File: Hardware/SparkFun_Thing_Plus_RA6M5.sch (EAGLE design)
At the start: 109 parts, among them J1 USB Female Type C Connector, J2 THING_PLUS_LOGICAL, J3 QWIIC_RA, J4 CONN_03X2, J7 MICRO-SDFRICTION, Q1 20V/4.2A/52mΩ/1.4W, Q2 20V/4.2A/52mΩ/1.4W, U1 R7FA6M5, U2 DA14531MOD, U3 MCP73831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

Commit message: Update for Reds.
Change QSPI flash chip to same one as Portenta C33
Remove boot button
Move reset button to space it out
Add boot test point
Recenter programming header silk
Update GPIO silk
Rename nets in schematic
Remove BLE Reset jumper
Remove DNP caps from 24MHz xtal
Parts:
- removed C7, C8: DNP, SparkFun-Capacitors:DNP-0402-TIGHT_NO_CREAM
- removed RST: JUMPER-SMT_2_NC_TRACE_SILK, SparkFun-Jumpers:JUMPER-SMT_2_NC_TRACE_SILK
- removed S1: BOOT, SparkFun-Switches:MOMENTARY-SWITCH-SPST-SMD-4.6X2.8MM
- added TP10: TEST-POINT3X5, SparkFun-Connectors:TEST-POINT3X5
- FRAME1, FRAME2: REV v01 -> v10
- U5: value W25QXX128MBIT-6X5 -> MX25L12833F 128Mb; device SparkFun-IC-Memory:W25QXX128MBIT-6X5 -> SparkFun-IC-Memory:MX25L12833F_128MBIT_QSPI
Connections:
- net A0 renamed A0/DAC0/D7
- net A1 renamed A1/DAC1/D8
- net A2 renamed A2/D9
- net A3 renamed A3/D10
- net A4 renamed A4/D11
- net A5 renamed A5/D12
- net DA14531_RST renamed BLE_RST
- net FREE renamed FREE/D30
- net GPIO0/!CS! renamed GPIO0/!CS!/D0
- net GPIO1 renamed GPIO1/D1
- net GPIO2 renamed GPIO2/D2
- net GPIO3 renamed GPIO3/D3
- net GPIO4 renamed GPIO4/D4
- net GPIO5 renamed GPIO5/D5
- net GPIO6 renamed GPIO6/D6
- net RA6_SWO/TDO/PICO renamed RA6_SWO/TDO/PICO/D18
- net RA6_TDI/POCI renamed RA6_TDI/POCI/D17
- net SCK renamed SCK/D19
- net SCL renamed SCL/D16
- net SDA renamed SDA/D15
- net UART_RX renamed UART_RX/D21
- net UART_TX renamed UART_TX/D20
- removed net N$25: RST.2, U1G1.P115/SSITXD0_B/GTIOC4A
- net !DA14531_RST!: now also U1G1.P115/SSITXD0_B/GTIOC4A; no longer RST.1
- net BOOT/MD: now also TP10.1; no longer S1.2
- net EXTAL: no longer C7.2
- net GND: no longer S1.1
- net GND_24: no longer C7.1, C8.1
- net QIO3: now also U5.D3/!RESET!; no longer U5.D3/!HOLD!
- net XTAL: no longer C8.2
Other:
- note added: "To load a new bootloader, pull BOOT/MD low. To load new Arduino code, double tap reset button."
- note removed: "Cut RST trace to remove BLE module reset capability. In case doing this causes a boot loop. To be removed or disabled in reds."
- moved on the sheet: R14, R8, S2

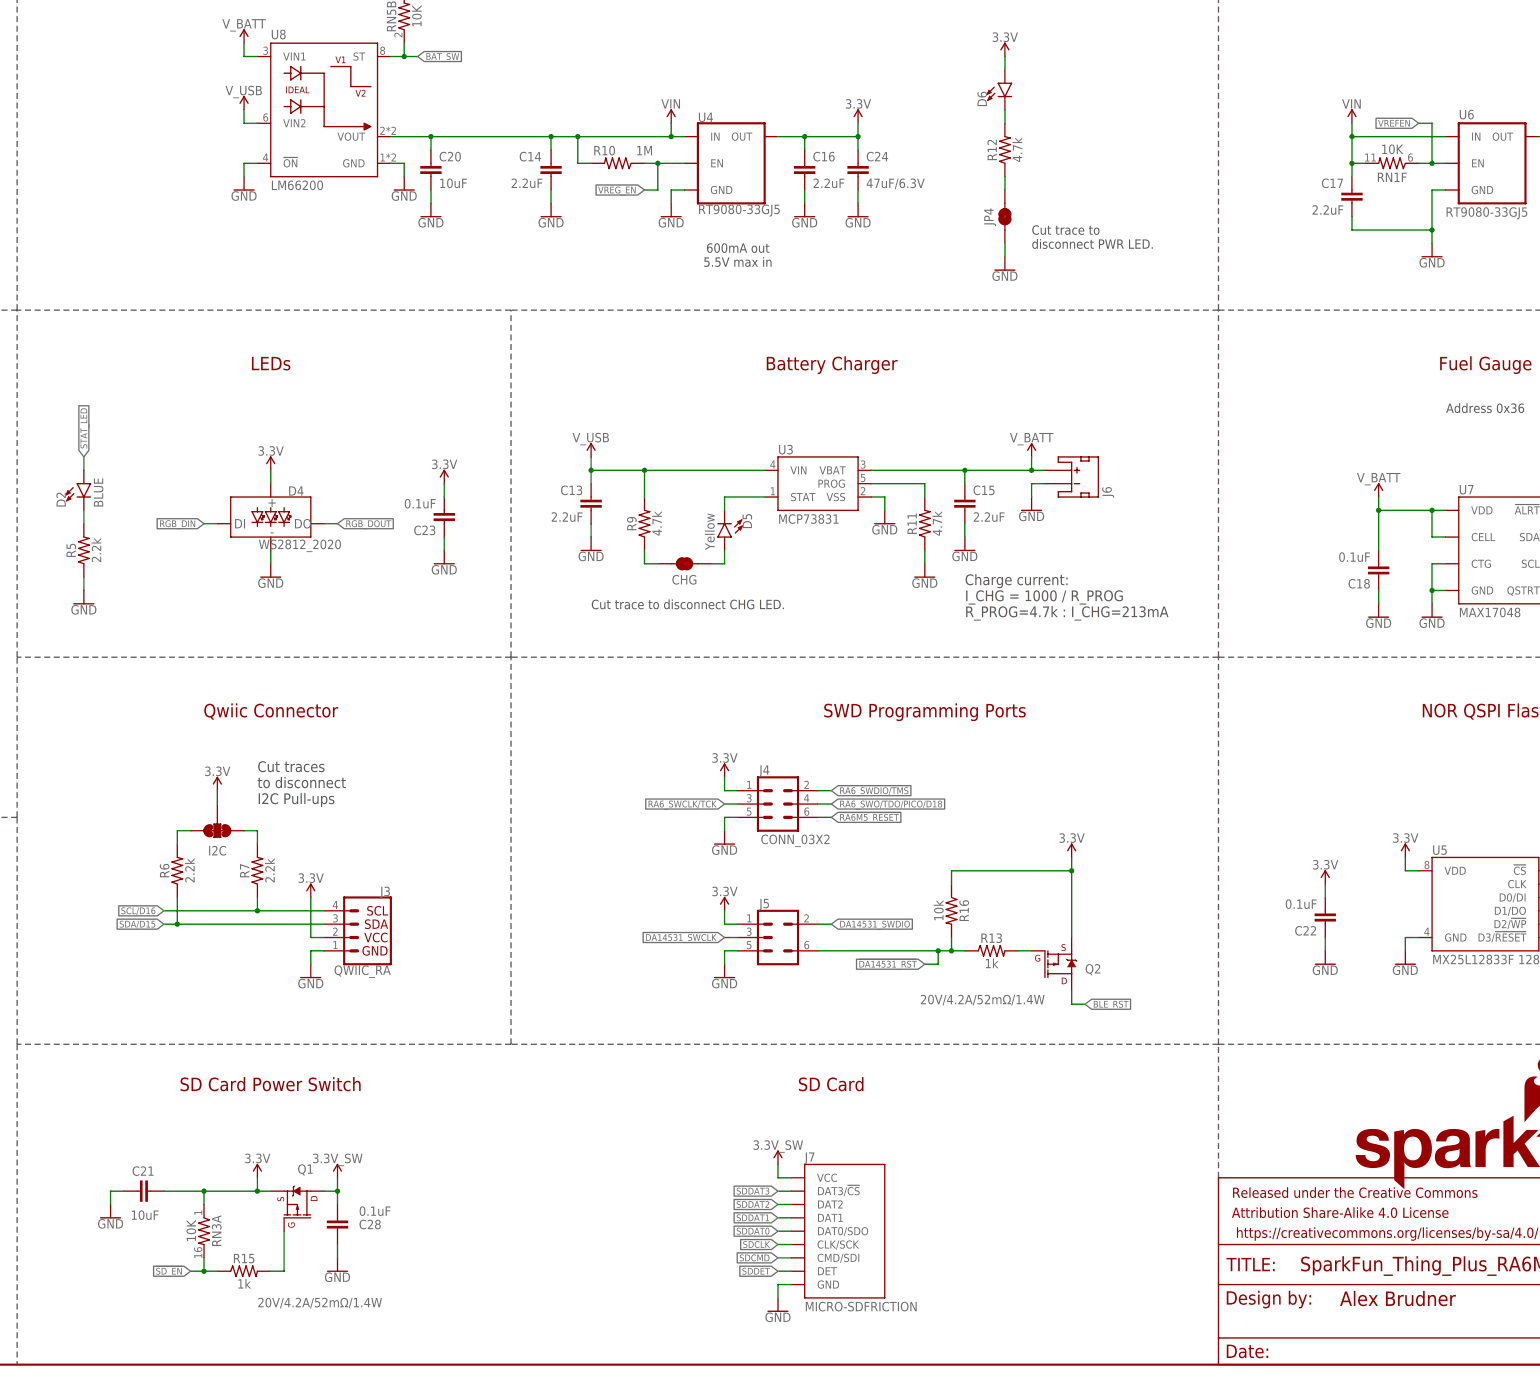
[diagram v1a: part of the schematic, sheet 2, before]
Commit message: V10 hardware post reds review update
Connect fills on bottom side near bottom diamond.
Add user button near reset button.
VREF EN now pulls up to 3.3V instead of VIN.
Change VREF silk bottom side to inverted VA.
Update EN and !RST! silk flags to use the right arrow.
Move vias to allow fills.
Adjust guard trace around Y1 to accommodate removing caps.
Add ground vias near QSPI data lines where possible.
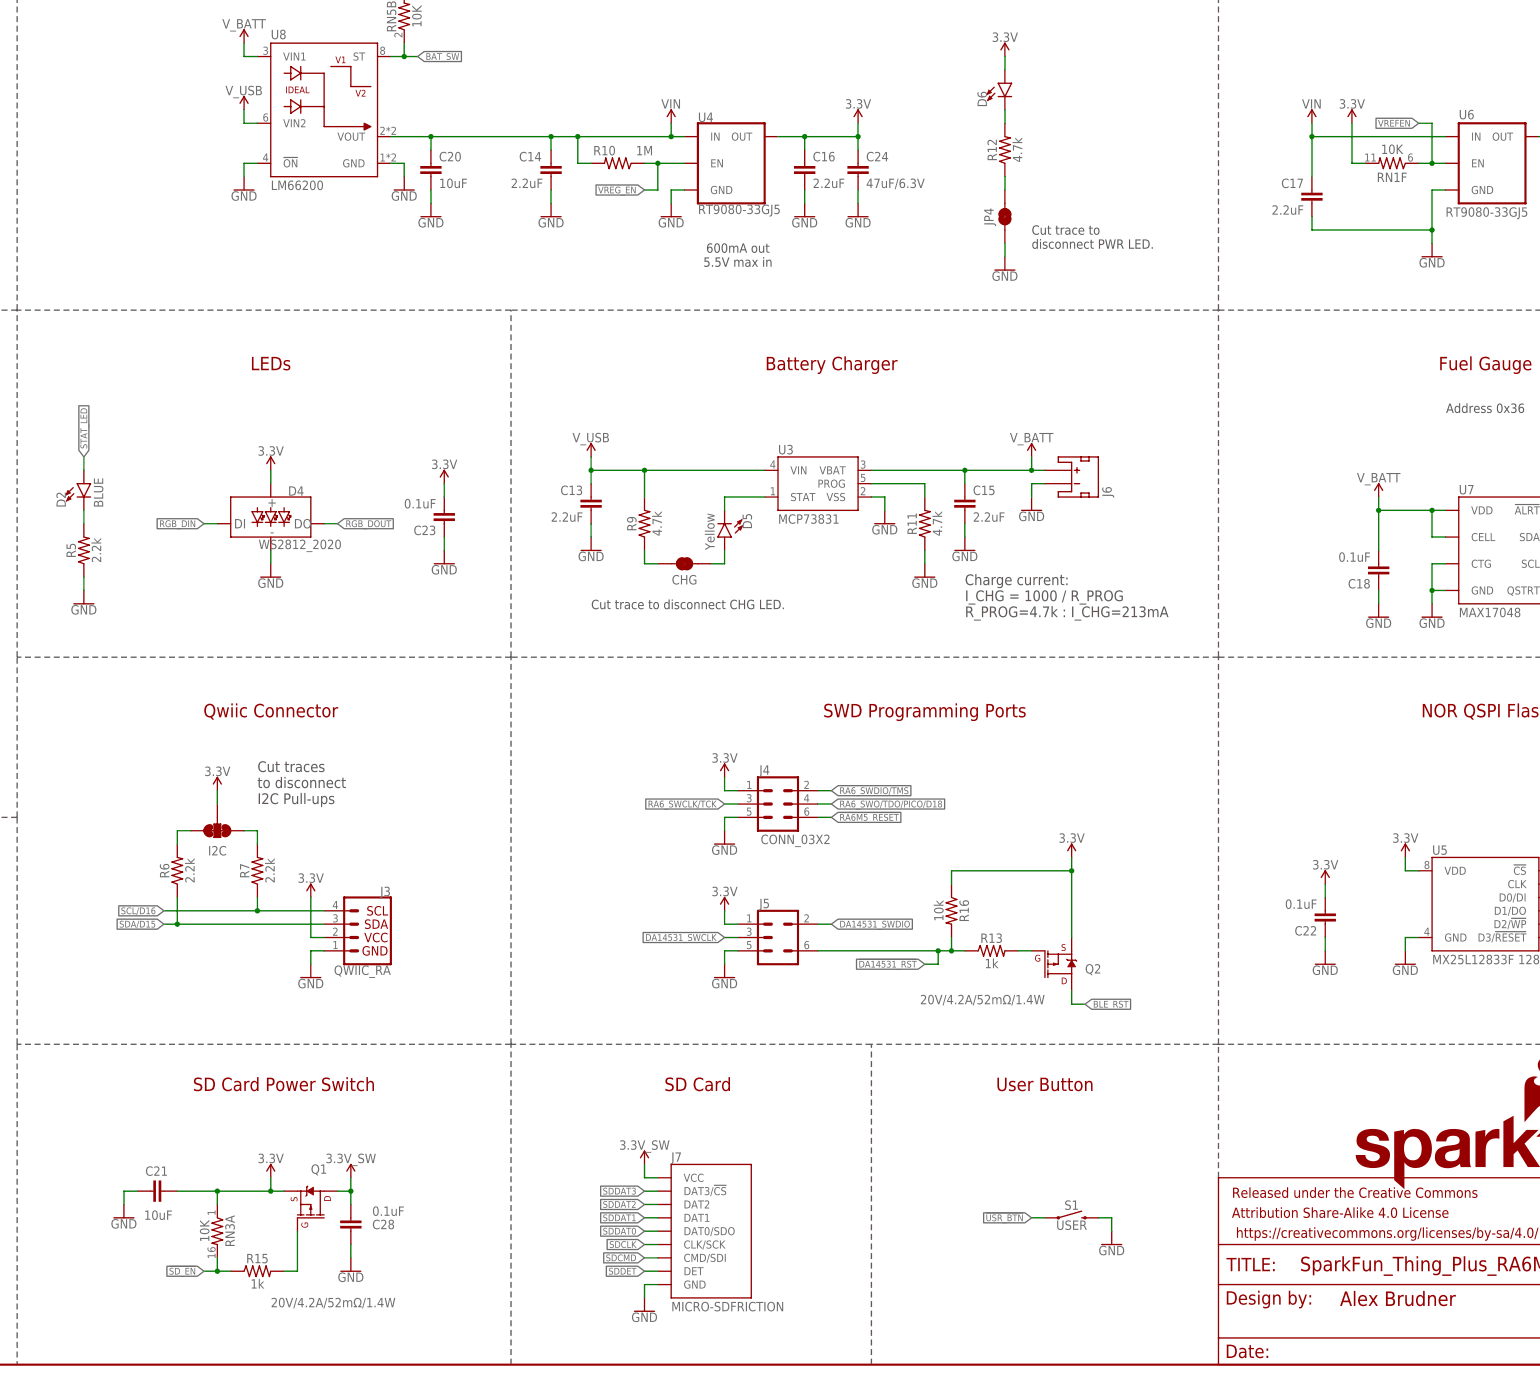
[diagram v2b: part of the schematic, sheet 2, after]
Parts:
- added S1: USER, SparkFun-Switches:MOMENTARY-SWITCH-SPST-SMD-4.6X2.8MM
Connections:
- removed net N$12: RN3B.2, U1G1.P415/USB_VBUSEN/SCL2/SSLB2_B
- new net !USR_BTN!: RN3B.2, S1.1, U1G1.P415/USB_VBUSEN/SCL2/SSLB2_B
- net 3.3V: now also RN1F.2, RN3B.1
- net GND: now also S1.2; no longer RN3B.1
- net VIN: no longer RN1F.2
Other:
- note added: "User Button"
- moved on the sheet: C17, C21, C28, J7, Q1, R15, RN3A, RN3B
